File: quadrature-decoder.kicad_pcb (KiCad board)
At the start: 2 copper layers, 100 x 100 mm, 6 parts, among them J1 Screw_Terminal_01x05, J2 Conn_02x20_Counter_Clockwise, U1 4013, U2 4029, U3 4029, U4 4029

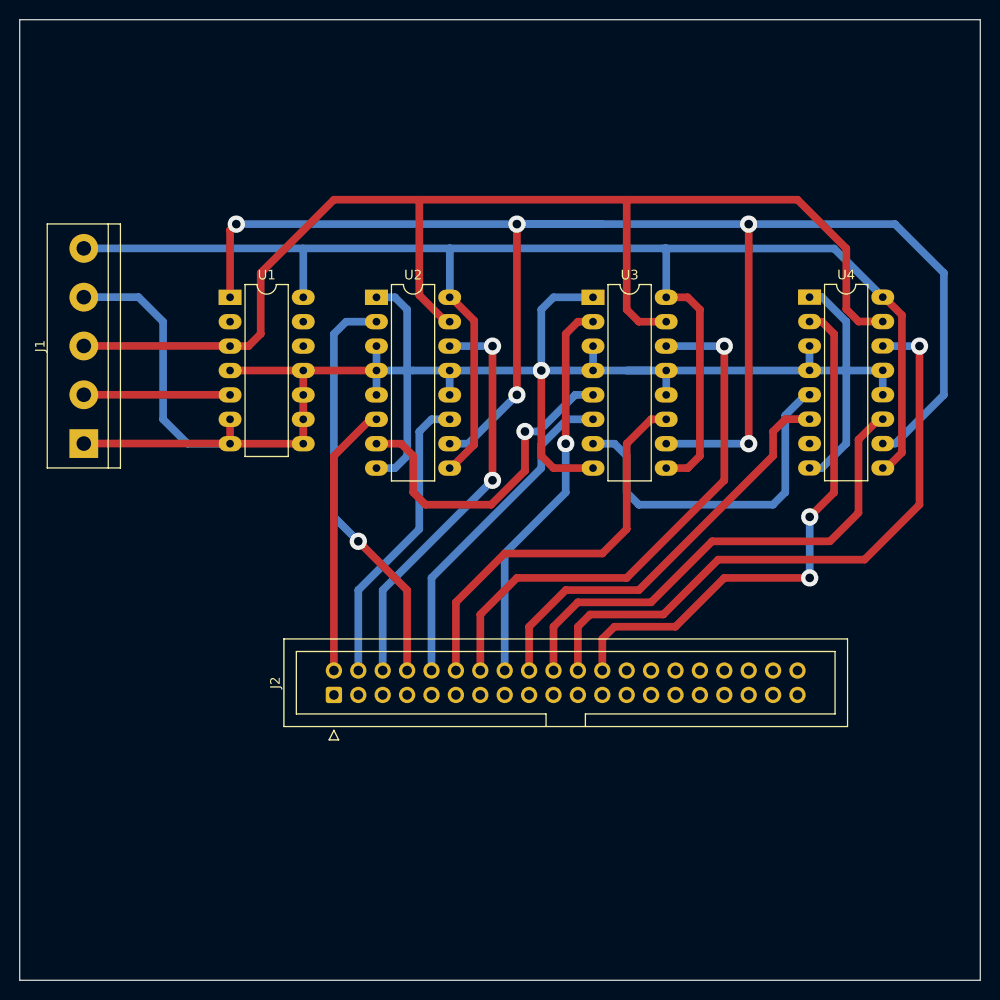
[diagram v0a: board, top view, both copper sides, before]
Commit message: Improve routing and component positioning; add capacitors
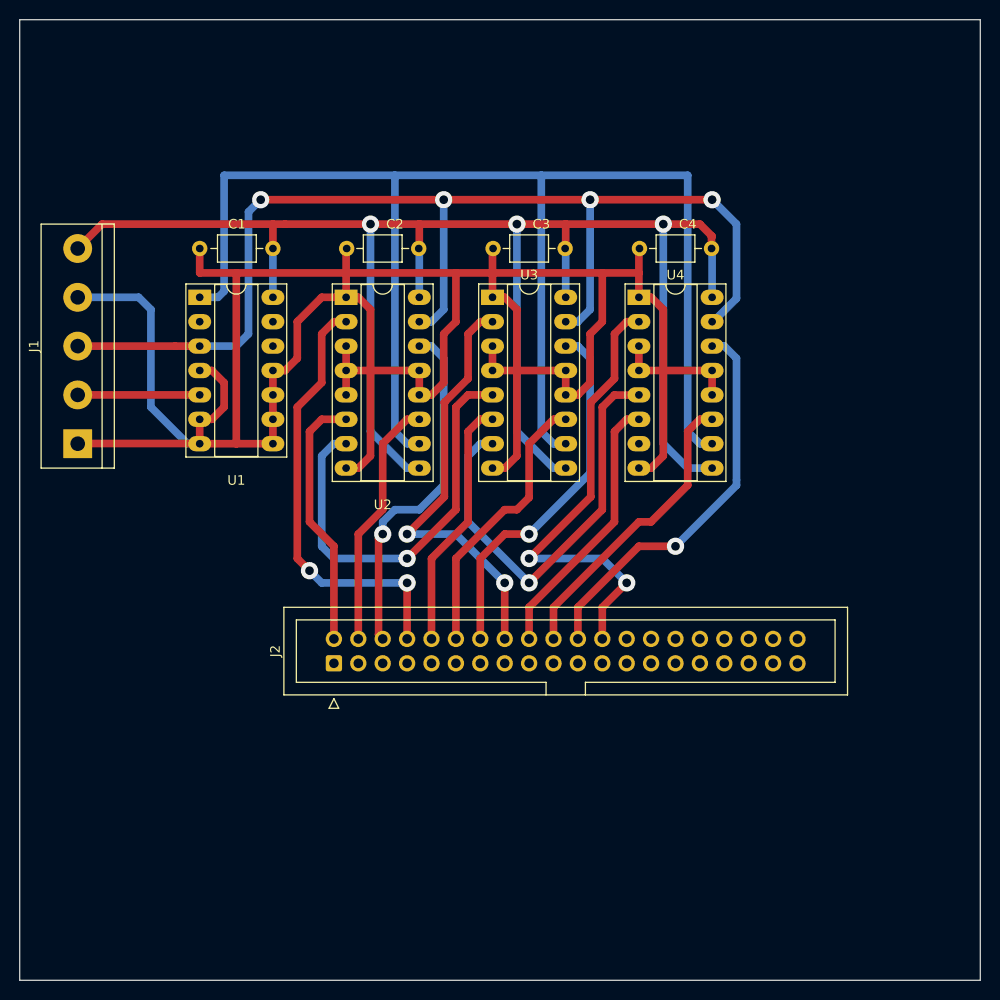
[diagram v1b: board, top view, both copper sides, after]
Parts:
- added C1: 100nF, Capacitor_THT:C_Axial_L3.8mm_D2.6mm_P7.50mm_Horizontal, F.Cu at (86.4, 83.8)
- added C2: 100nF, Capacitor_THT:C_Axial_L3.8mm_D2.6mm_P7.50mm_Horizontal, F.Cu at (101.5, 83.8)
- added C3: 100nF, Capacitor_THT:C_Axial_L3.8mm_D2.6mm_P7.50mm_Horizontal, F.Cu at (116.8, 83.8)
- added C4: 100nF, Capacitor_THT:C_Axial_L3.8mm_D2.6mm_P7.50mm_Horizontal, F.Cu at (132.0, 83.8)
- U1: footprint Package_DIP:DIP-14_W7.62mm_LongPads -> Package_DIP:DIP-14_W7.62mm_Socket_LongPads
- U2, U3, U4: footprint Package_DIP:DIP-16_W7.62mm_LongPads -> Package_DIP:DIP-16_W7.62mm_Socket_LongPads
- moved U4 17.8 mm to (124.5, 88.9)
- moved U3 10.5 mm to (109.2, 88.9)
- moved J2 3.29 mm to (92.7, 127.0)
- moved U1 3.16 mm to (78.7, 88.9)
- moved U2 3.16 mm to (94.0, 88.9)
- moved J1 0.64 mm to (66.0, 104.1)
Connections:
- J1 pad 2: Vss -> /ENC_B
- J1 pad 3: Vss -> /ENC_A
- U1 pad 3: Vss -> /ENC_A
- U1 pad 5: Vss -> /ENC_B
- U2 pad 15: Vss -> /ENC_A
- U3 pad 15: Vss -> /ENC_A
- U4 pad 15: Vss -> /ENC_A
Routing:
- net /ENC_A: track 0.00 -> 123.7 mm, vias 0 -> 4
- net Vss: track 368.7 -> 291.4 mm, vias 1 -> 0
- net Net-(J2-Pad22): track 65.7 -> 41.3 mm
- net Net-(J2-Pad20): track 52.3 -> 31.2 mm
- net Net-(U1-Pad1): track 172.1 -> 152.3 mm, vias 5 -> 0
- net Net-(J2-Pad14): track 57.0 -> 38.5 mm
- net Vdd: track 163.9 -> 182.5 mm, vias 0 -> 3
- net Net-(J2-Pad18): track 44.2 -> 28.3 mm
- net Net-(J2-Pad12): track 42.1 -> 29.1 mm
- net /ENC_B: track 0.00 -> 12.7 mm
- net Net-(U2-Pad7): track 34.5 -> 44.1 mm
- net Net-(J2-Pad24): track 57.1 -> 48.2 mm
- net Net-(J2-Pad10): track 34.7 -> 26.2 mm
- net Net-(U3-Pad7): track 36.8 -> 44.7 mm, vias 0 -> 1
- net Net-(J2-Pad6): track 43.0 -> 36.8 mm, vias 2 -> 1
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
